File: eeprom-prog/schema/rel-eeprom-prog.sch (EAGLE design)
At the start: 4 parts, among them IC2 74HC595N, IC3 74HC595N

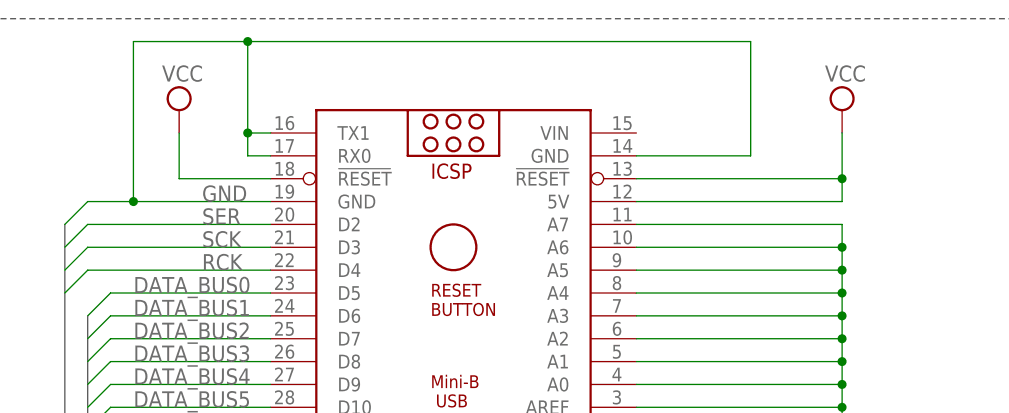
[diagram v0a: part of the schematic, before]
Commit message: Removed reset pull up for eeprom prog
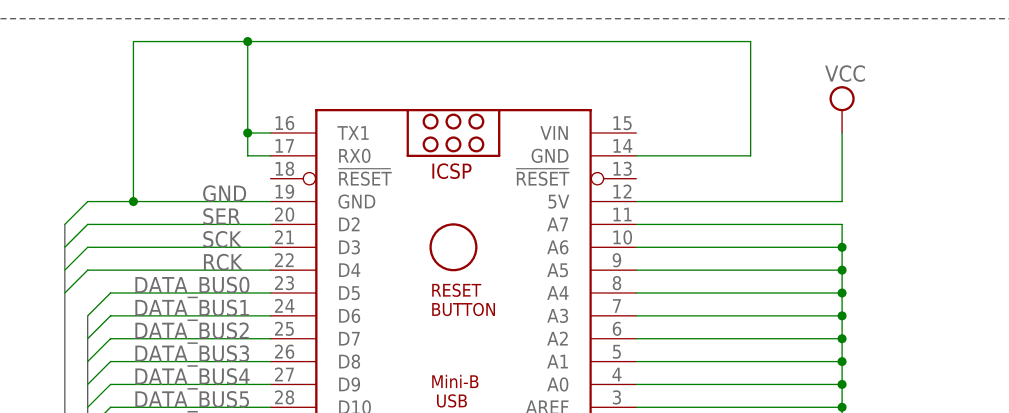
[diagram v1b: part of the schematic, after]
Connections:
- net VCC: no longer ARDUINO_NANO1.!RESET@1, ARDUINO_NANO1.!RESET@2
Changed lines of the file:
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@@
 <part name="GND4" library="supply1" library_urn="urn:adsk.eagle:library:371" deviceset="GND" device=""/>
 <part name="SUPPLY1" library="supply2" library_urn="urn:adsk.eagle:library:372" deviceset="VCC" device=""/>
-<part name="SUPPLY2" library="supply2" library_urn="urn:adsk.eagle:library:372" deviceset="VCC" device=""/>
 <part name="GND1" library="supply1" library_urn="urn:adsk.eagle:library:371" deviceset="GND" device=""/>
 <part name="GND5" library="supply1" library_urn="urn:adsk.eagle:library:371" deviceset="GND" device=""/>
@@
 <instance part="GND4" gate="1" x="45.72" y="-17.78"/>
 <instance part="SUPPLY1" gate="G$1" x="58.42" y="116.84"/>
-<instance part="SUPPLY2" gate="G$1" x="-15.24" y="116.84"/>
 <instance part="GND1" gate="1" x="58.42" y="76.2"/>
 <instance part="GND5" gate="1" x="45.72" y="-2.54"/>
@@
 <pinref part="ARDUINO_NANO1" gate="G$1" pin="5V"/>
 <wire x1="35.56" y1="106.68" x2="58.42" y2="106.68" width="0.1524" layer="91"/>
-<wire x1="58.42" y1="106.68" x2="58.42" y2="109.22" width="0.1524" layer="91"/>
 <pinref part="SUPPLY1" gate="G$1" pin="VCC"/>
-<pinref part="ARDUINO_NANO1" gate="G$1" pin="!RESET@2"/>
-<wire x1="58.42" y1="109.22" x2="58.42" y2="114.3" width="0.1524" layer="91"/>
-<wire x1="35.56" y1="109.22" x2="58.42" y2="109.22" width="0.1524" layer="91"/>
-<junction x="58.42" y="109.22"/>
-</segment>
-<segment>
-<pinref part="ARDUINO_NANO1" gate="G$1" pin="!RESET@1"/>
-<wire x1="-5.08" y1="109.22" x2="-15.24" y2="109.22" width="0.1524" layer="91"/>
-<wire x1="-15.24" y1="109.22" x2="-15.24" y2="114.3" width="0.1524" layer="91"/>
-<pinref part="SUPPLY2" gate="G$1" pin="VCC"/>
-</segment>
-</net>
+<wire x1="58.42" y1="106.68" x2="58.42" y2="114.3" width="0.1524" layer="91"/>
+</segment>
+</net>
